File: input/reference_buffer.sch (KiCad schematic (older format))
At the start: 32 parts, among them Q1 NSS1C300ET4G, U1 OP27, U10 OP27

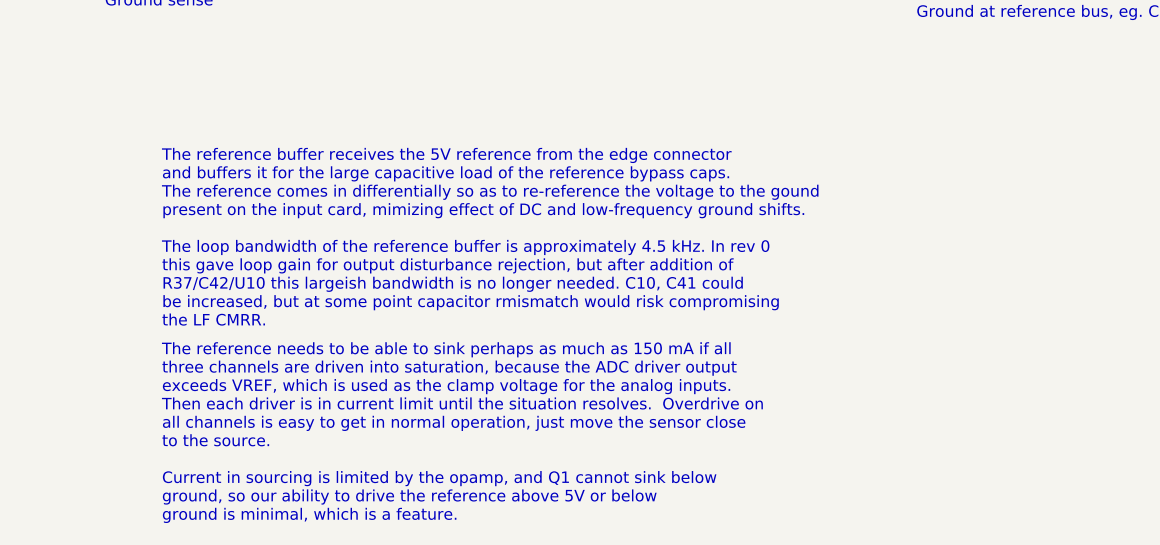
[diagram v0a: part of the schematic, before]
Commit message: More work on dac/power.sch and dac/reference_buffer.sch. Also, fixed comments in input/reference_buffer.sch
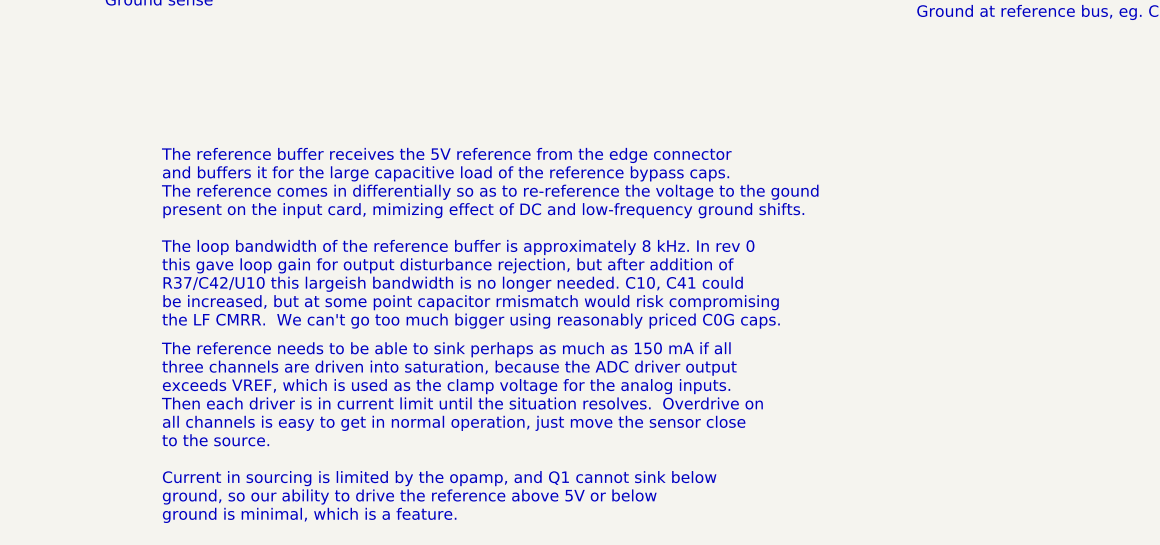
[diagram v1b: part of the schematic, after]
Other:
- note added: "The reference buffer receives the 5V reference from the edge connector\nand buffers it for the large capacitive load of the reference bypass caps. \nThe reference comes in differentially so as to re-reference the voltage to the gound\npresent on the input card, mimizing effect of DC and low-frequency ground shifts.\n\nThe loop bandwidth of the reference buffer is approximately 8 kHz. In rev 0\nth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"
- note removed: "The reference buffer receives the 5V reference from the edge connector\nand buffers it for the large capacitive load of the reference bypass caps. \nThe reference comes in differentially so as to re-reference the voltage to the gound\npresent on the input card, mimizing effect of DC and low-frequency ground shifts.\n\nThe loop bandwidth of the reference buffer is approximately 4.5 kHz. In rev 0\n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"
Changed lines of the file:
@@
 $EndComp
 Text Notes 6250 5950 0    50   ~ 0
-The reference buffer receives the 5V reference from the edge connector\nand buffers it for the large capacitive load of the reference bypass caps. \nThe reference comes in differentially so as to re-reference the voltage to the gound\npresent on the input card, mimizing effect of DC and low-frequency ground shifts.\n\nThe loop bandwidth of the reference buffer is approximately 4.5 kHz. In rev 0\nthis gave loop gain for output disturbance rejection, but after addition of \nR37/C42/U10 this largeish bandwidth is no longer needed. C10, C41 could\nbe increased, but at some point capacitor rmismatch would risk compromising \nthe LF CMRR.
+The reference buffer receives the 5V reference from the edge connector\nand buffers it for the large capacitive load of the reference bypass caps. \nThe reference comes in differentially so as to re-reference the voltage to the gound\npresent on the input card, mimizing effect of DC and low-frequency ground shifts.\n\nThe loop bandwidth of the reference buffer is approximately 8 kHz. In rev 0\nthis gave loop gain for output disturbance rejection, but after addition of \nR37/C42/U10 this largeish bandwidth is no longer needed. C10, C41 could\nbe increased, but at some point capacitor rmismatch would risk compromising \nthe LF CMRR.  We can't go too much bigger using reasonably priced C0G caps.
 $Comp
 L Device:C_Small C?

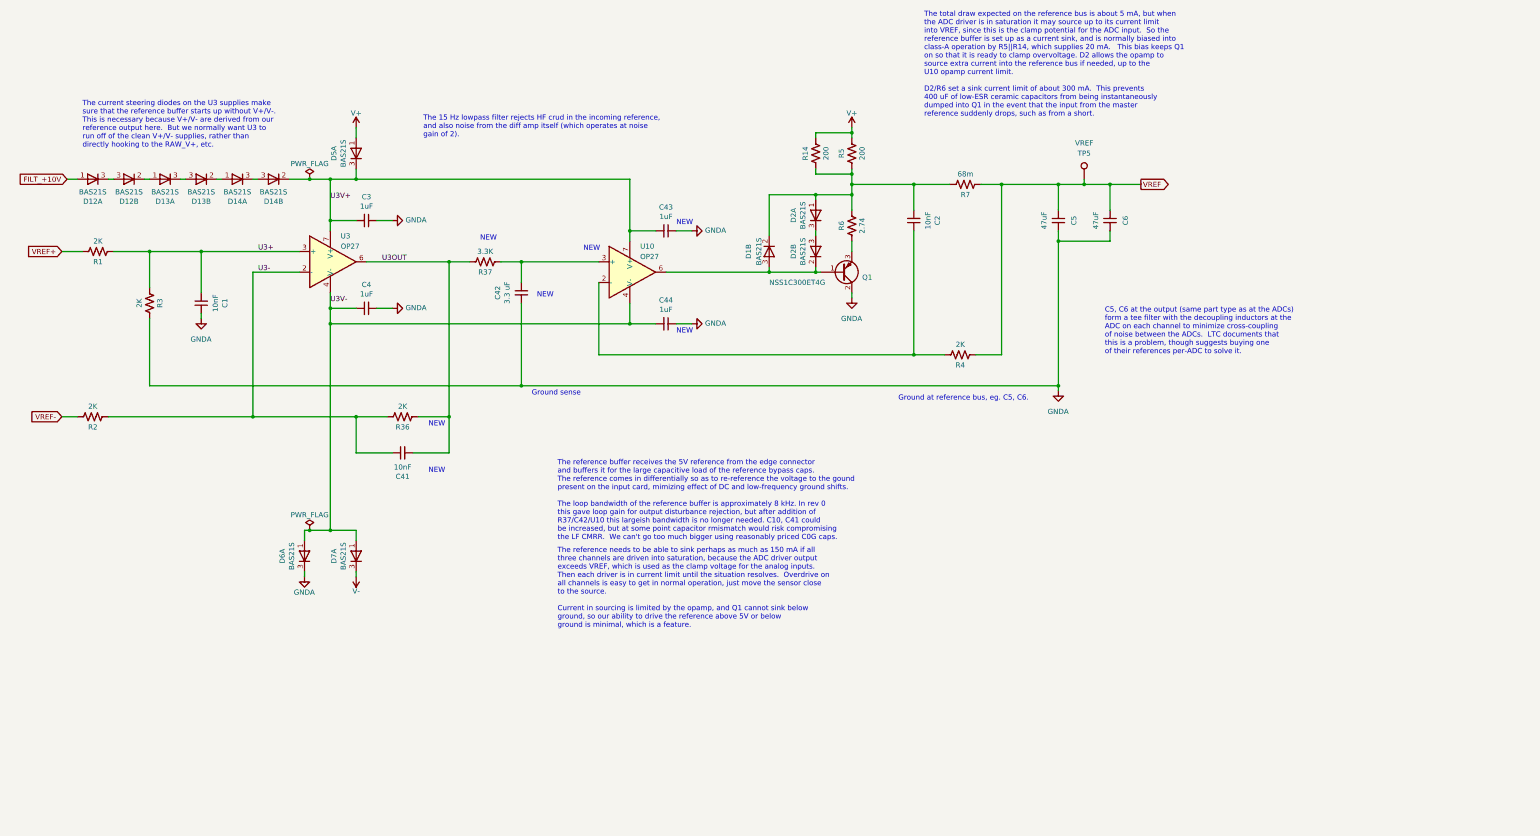
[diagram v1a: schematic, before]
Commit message: BOM change to dac/, start of board revision in input/adc.sch
dac: changed 10 Ohm MPN on BOM

input:
Fixed SOIC-8 footprints
Got rid of bootstrapping of the reference buffer.  Now it runs from the 10 Ohm/330 uF filtered +8/-6.
Changed power input beads from 22 Ohm to 180 Ohm.
Added diode clamp between GND and Earth grounds.
Changed reference buffer to dual opamp.
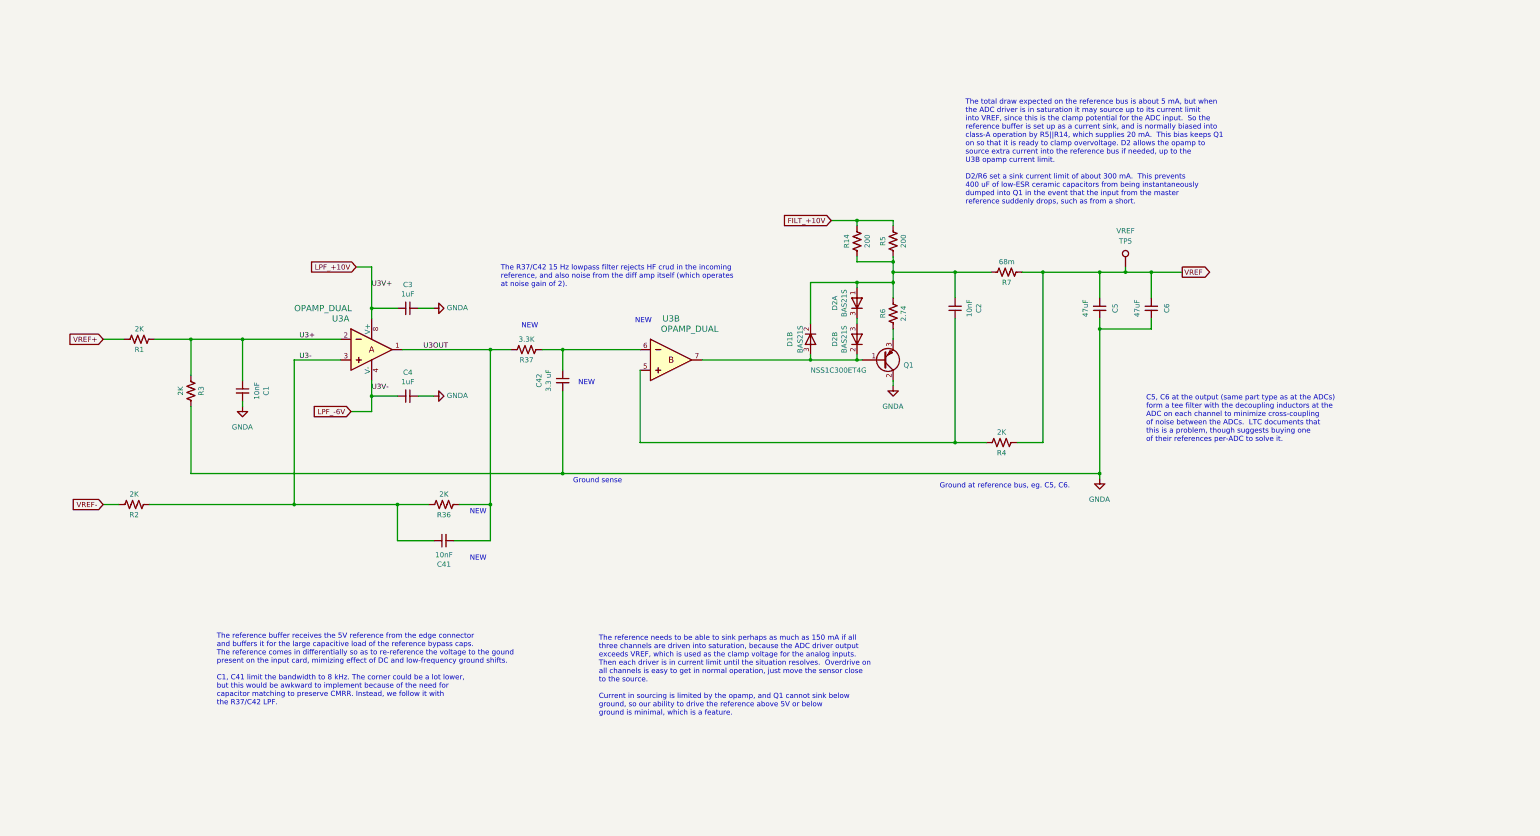
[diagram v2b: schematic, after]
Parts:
- removed C43, C44: 1uF, Capacitor_SMD:C_0805_2012Metric, symbol Device:C_Small
- removed D12, D13, D14, D5, D6, D7: BAS21S, Package_TO_SOT_SMD:SOT-23, symbol ilemt_input:BAS21S
- removed U1, U10: OP27, Package_SO:SOIC-8_3.9x4.9mm_P1.27mm, symbol ilemt_input:opamp_single
- added U3: OPAMP_DUAL, symbol ilemt_input:OPAMP_DUAL
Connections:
- net V+ is gone; now on net FILT_+10V: R14.2, R5.2
- net U3+: now also U3.2
- net U3-: now also U3.3
- net U3OUT: now also U3.1
- net at C2.1, R4.2: now also U3.5
- net at D1.2 (K), D2.3 (A), Q1.1 (B): now also U3.7
- net at C42.1, R37.1: now also U3.6
- net U3V+ renamed LPF_+10V
- net LPF_+10V: now also U3.8 (V+)
- net U3V- renamed LPF_-6V
- net LPF_-6V: now also U3.4 (V-)
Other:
- note added: "The R37/C42 15 Hz lowpass filter rejects HF crud in the incoming \nreference, and also noise from the diff amp itself (which operates\nat noise gain of 2)."
- note added: "The reference buffer receives the 5V reference from the edge connector\nand buffers it for the large capacitive load of the reference bypass caps. \nThe reference comes in differentially so as to re-reference the voltage to the gound\npresent on the input card, mimizing effect of DC and low-frequency ground shifts.\n\nC1, C41 limit the bandwidth to 8 kHz. The corner could be a lot lower,\nbut thi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"
- note removed: "The 15 Hz lowpass filter rejects HF crud in the incoming reference,\nand also noise from the diff amp itself (which operates at noise\ngain of 2)."
- note removed: "The current steering diodes on the U3 supplies make\nsure that the reference buffer starts up without V+/V-.\nThis is necessary because V+/V- are derived from our\nreference output here. But we normally want U3 to\nrun off of the clean V+/V- supplies, rather than\ndirectly hooking to the RAW_V+, etc."
- note removed: "The reference buffer receives the 5V reference from the edge connector\nand buffers it for the large capacitive load of the reference bypass caps. \nThe reference comes in differentially so as to re-reference the voltage to the gound\npresent on the input card, mimizing effect of DC and low-frequency ground shifts.\n\nThe loop bandwidth of the reference buffer is approximately 8 kHz. In rev 0\nth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"
- moved on the sheet: C1, C2, C3, C4, C41, C42, C5, C6, D1B, D2A, D2B, Q1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

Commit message: Fix to swapped opamp pins in reference_buffer.sch, assigned opamp type, annotated.  Improved comments. Other changes are almost entirely kicad inflicted spurious modifications of multi-instance sub-sheets.
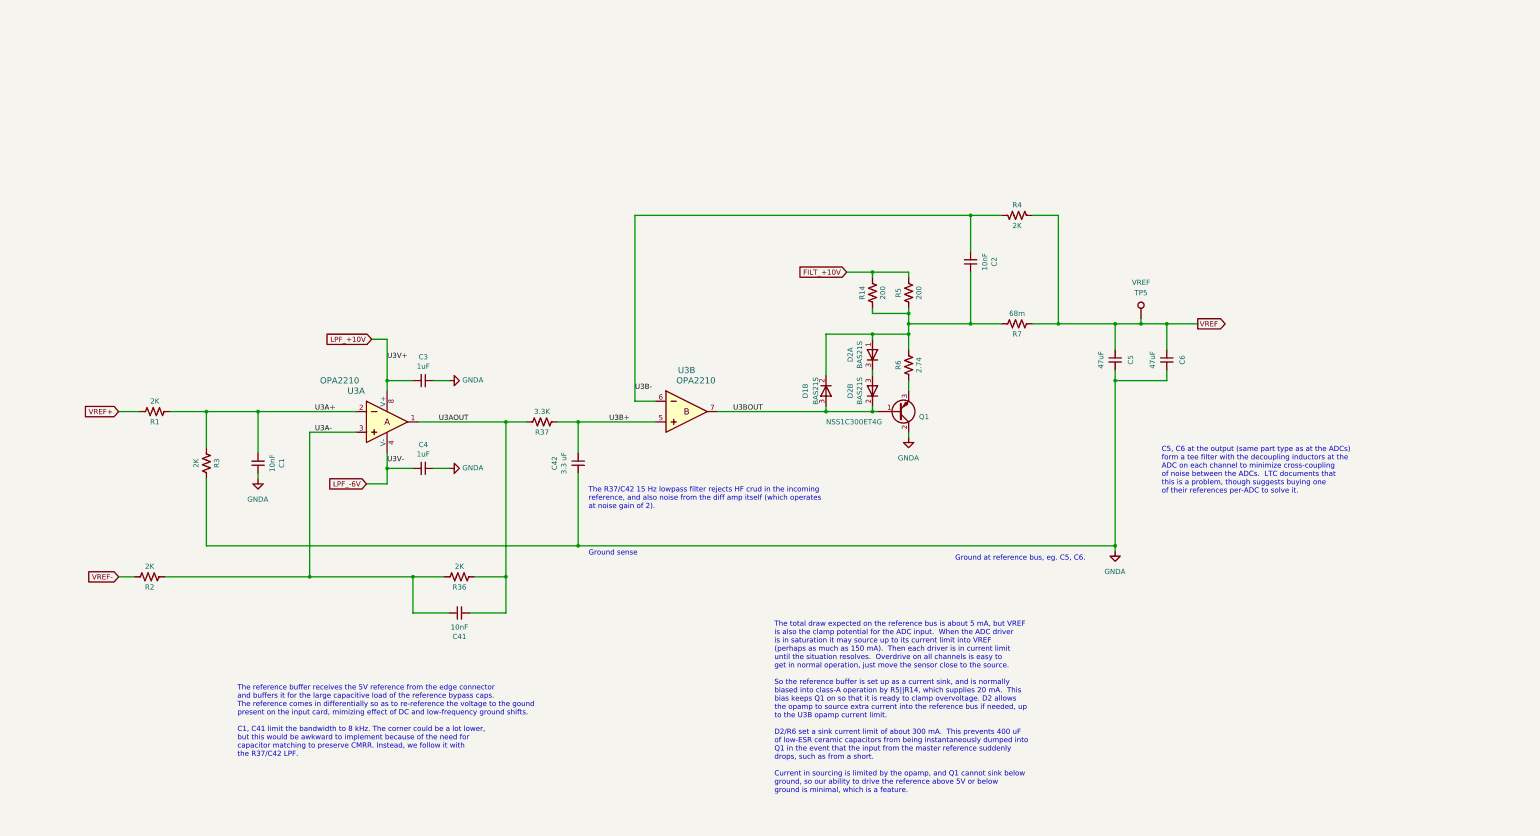
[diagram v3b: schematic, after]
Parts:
- U3: value OPAMP_DUAL -> OPA2210; footprint (none) -> Package_SO:SOIC-8_3.9x4.9mm_P1.27mm
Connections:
- net U3B-: now reaches C2.1, R4.2
- net U3B-: now also U3.6; no longer U3.5
- net U3BOUT: now reaches D1.2 (K), D2.3 (A), Q1.1 (B), U3.7
- net U3B+: now reaches C42.1, R37.1
- net U3B+: now also U3.5; no longer U3.6
- net U3+ renamed U3A+
- net U3- renamed U3A-
- net U3OUT renamed U3AOUT
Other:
- note added: "The total draw expected on the reference bus is about 5 mA, but VREF\nis also the clamp potential for the ADC input. When the ADC driver\nis in saturation it may source up to its current limit into VREF\n(perhaps as much as 150 mA). Then each driver is in current limit\nuntil the situation resolves. Overdrive on all channels is easy to\nget in normal operation, just move the sensor close to the s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"
- note removed: "NEW"
- note removed: "The reference needs to be able to sink perhaps as much as 150 mA if all \nthree channels are driven into saturation, because the ADC driver output\nexceeds VREF, which is used as the clamp voltage for the analog inputs. \nThen each driver is in current limit until the situation resolves. Overdrive on\nall channels is easy to get in normal operation, just move the sensor close \nto the source.\n\n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"
- note removed: "The total draw expected on the reference bus is about 5 mA, but when\nthe ADC driver is in saturation it may source up to its current limit\ninto VREF, since this is the clamp potential for the ADC input. So the\nreference buffer is set up as a current sink, and is normally biased into \nclass-A operation by R5||R14, which supplies 20 mA. This bias keeps Q1\non so that it is ready to clamp overvo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"
- moved on the sheet: C1, C2, C3, C4, C41, C42, C5, C6, D1B, D2A, D2B, Q1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
